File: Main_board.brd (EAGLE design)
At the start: 77.5 x 67.3 mm, 65 parts, among them U2 TPS61200, U3 MAX1704X, U4 USD-SOCKETNEW, U5 TPS61200, X1 USB-MICROB, Y1 16MHz KX-7

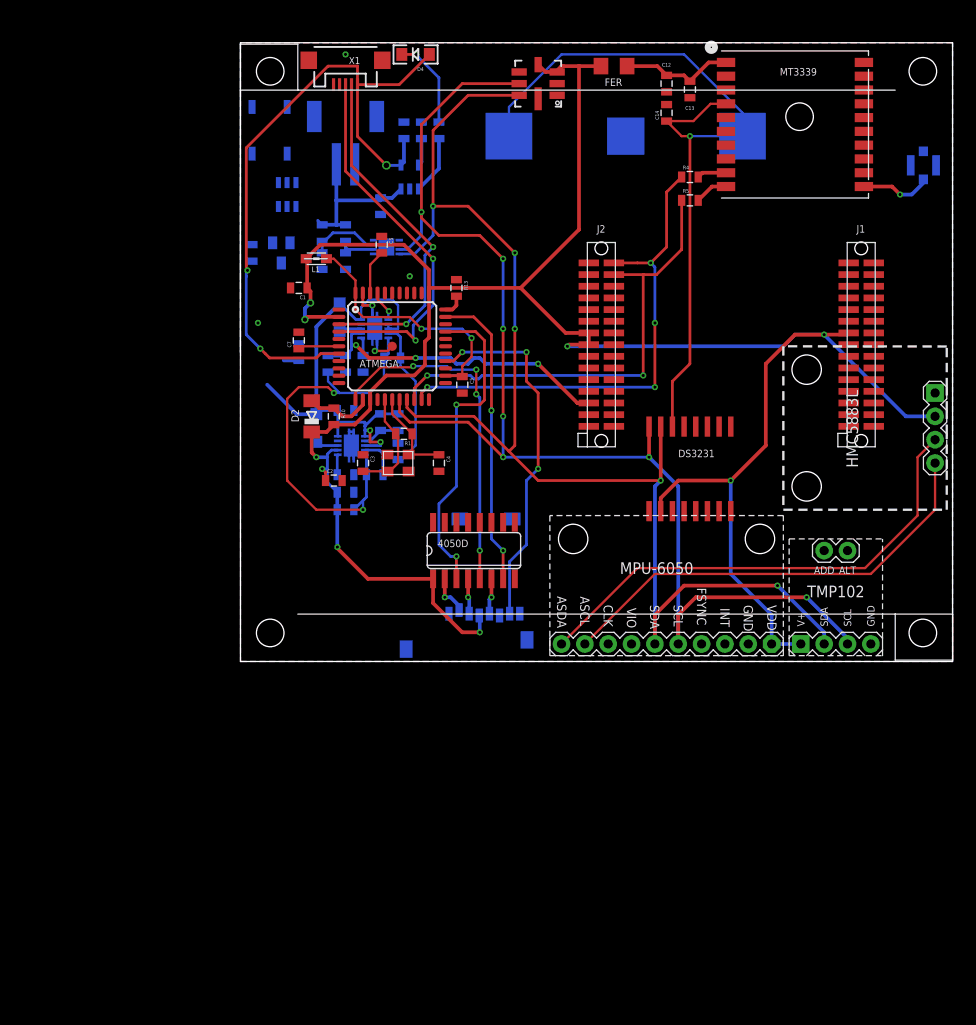
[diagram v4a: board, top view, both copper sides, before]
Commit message: 3V3 boost converter replacement
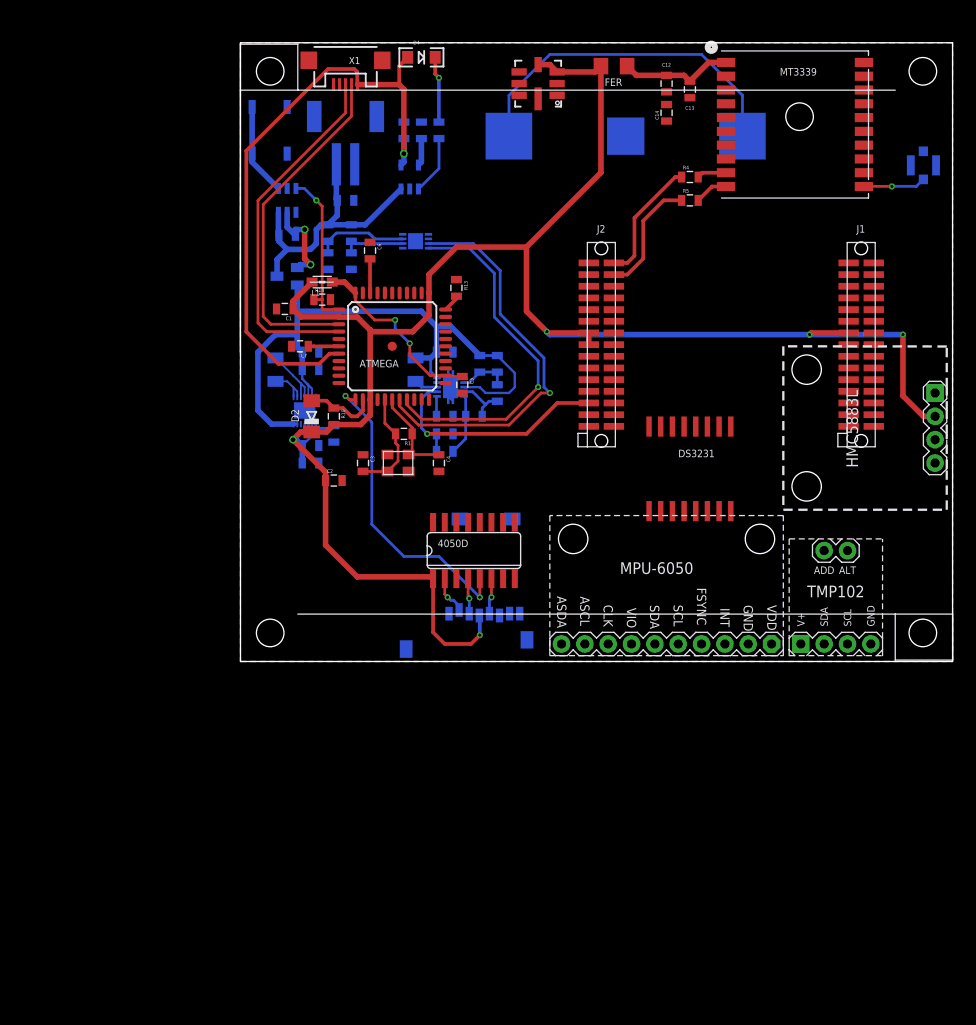
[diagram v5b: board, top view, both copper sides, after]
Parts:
- removed C22: 22uF, SparkFun:0805
- removed C24: 0.1uF, SparkFun:0805
- removed L3: 4.7uH, 1.2A, SparkFun:CDRH2D09
- removed R20: 2M, SparkFun:0805
- removed R21: 220k, SparkFun:0805
- removed U5: TPS61200, SparkFun:QFN-10_PAD
- added C19, C20, C21, C23: 22uF, SparkFun:0805
- added C25: 0.1uF, SparkFun:0805
- added L4: 4.7uH, 1.2A, rcl:2520
- added MAX16054: MAX16054, maxim:SOT23-6L
- L2: device SparkFun:CDRH2D09 -> rcl:2520
- R7: value 1.2M -> 2M
- U$9: value MAX16054 -> MAX8625A; device maxim:SOT23-6L -> maxim:14-TDFN-EP
- moved U$9 23.6 mm to (6.99, 27.3), turned to 270 degrees
- moved C15 12.5 mm to (22.2, 26.7)
- moved C16 12.5 mm to (22.2, 33.7)
- moved C8 12.5 mm to (22.2, 24.8)
- moved L2 12.5 mm to (19.1, 31.8), turned to 270 degrees
- moved R6 12.5 mm to (27.9, 29.2)
- moved C11 12.5 mm to (26.0, 32.4)
- moved R3 12.5 mm to (27.9, 32.4)
- moved R7 12.5 mm to (22.2, 22.9)
- moved R8 12.5 mm to (25.4, 26.7)
- moved U2 12.5 mm to (22.9, 29.8)
- moved R18 6.25 mm to (8.89, 39.4), flipped to the top, turned to 0 degrees
- moved R11 4.26 mm to (5.08, 46.4), turned to 180 degrees
- moved C10 3.86 mm to (11.4, 50.2), turned to 180 degrees
- moved U3 3.24 mm to (19.1, 45.7)
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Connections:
- removed net N$16: L3.P$1, U5.3
- removed net N$17: C24.1, U5.1
- new net N$22: C25.1, U$9.P$9
- new net N$23: L4.P$1, U$9.P$2, U$9.P$3
- new net N$24: L4.P$2, U$9.P$4, U$9.P$5
- net 5V: now also C8.1, R7.2, U2.2; no longer C22.1, R20.2, U5.2
- net A5: now also U2.6; no longer U5.6
- net D7: now also MAX16054.3; no longer U$9.3
- net FB: no longer R20.1, R21.2, U5.10
- net GND: now also C19.2, C20.2, C21.2, C23.2, C25.2, MAX16054.2, U$9.P$12, U$9.P$13, U$9.P$8; no longer C22.2, C24.2, U$9.2, U5.11, U5.12, U5.13, U5.14, U5.15, U5.4
- net GND1: no longer R21.1, U5.9
- net N$15: now also MAX16054.1; no longer U$9.1
- net N$19: now also MAX16054.5; no longer U$9.4
- net VCC: now also C21.1, C23.1, U$9.P$10, U$9.P$11; no longer C8.1, R7.2, U$9.6, U2.2
- net VIN: now also C19.1, C20.1, U$9.P$14, U$9.P$15, U$9.P$6, U$9.P$7; no longer L3.P$2, U2.6, U5.5, U5.7, U5.8
- net V_BATT: now also MAX16054.6
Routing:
- net SDA: track 141.7 -> 39.6 mm, vias 5 -> 1
- net SCL: track 140.9 -> 43.9 mm, vias 7 -> 1
- net AUX_SDA: track 53.6 -> 0.00 mm
- net VCC: track 254.0 -> 203.8 mm, vias 9 -> 5
- net AUX_SCL: track 49.2 -> 0.00 mm
- net VEE: track 84.7 -> 38.0 mm, vias 1 -> 0
- net TX: track 54.8 -> 13.7 mm, vias 4 -> 0
- net IO12: track 39.5 -> 0.00 mm, vias 3 -> 0
- net FB: track 45.6 -> 6.62 mm, vias 2 -> 0
- net RX: track 51.8 -> 13.1 mm, vias 2 -> 0
- net IO10*: track 35.3 -> 0.00 mm, vias 2 -> 0
- net IO13*: track 32.9 -> 0.00 mm, vias 2 -> 0
- net VIN: track 51.9 -> 72.4 mm, vias 2 -> 0
- net GND1: track 22.7 -> 5.76 mm
- net D7: track 1.64 -> 17.6 mm, vias 0 -> 1
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
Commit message: Board routing + cleaning
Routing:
- net SDA: track 39.6 -> 131.9 mm, vias 1 -> 5
- net SCL: track 43.9 -> 125.4 mm, vias 1 -> 6
- net AUX_SDA: track 0.00 -> 49.8 mm, vias 0 -> 1
- net VEE: track 38.0 -> 86.8 mm, vias 0 -> 1
- net AUX_SCL: track 0.00 -> 46.3 mm, vias 0 -> 1
- net VCC: track 203.8 -> 249.7 mm, vias 5 -> 6
- net RX: track 13.1 -> 52.0 mm, vias 0 -> 2
- net IO12: track 0.00 -> 38.8 mm, vias 0 -> 1
- net IO10*: track 0.00 -> 38.6 mm, vias 0 -> 2
- net TX: track 13.7 -> 51.6 mm, vias 0 -> 2
- net IO13*: track 0.00 -> 36.3 mm, vias 0 -> 2
- net A5: track 0.00 -> 31.3 mm, vias 0 -> 3
- net GND: track 5.51 -> 6.46 mm
- net N$3: track 2.60 -> 3.25 mm
- net 5V: track 28.0 -> 28.5 mm

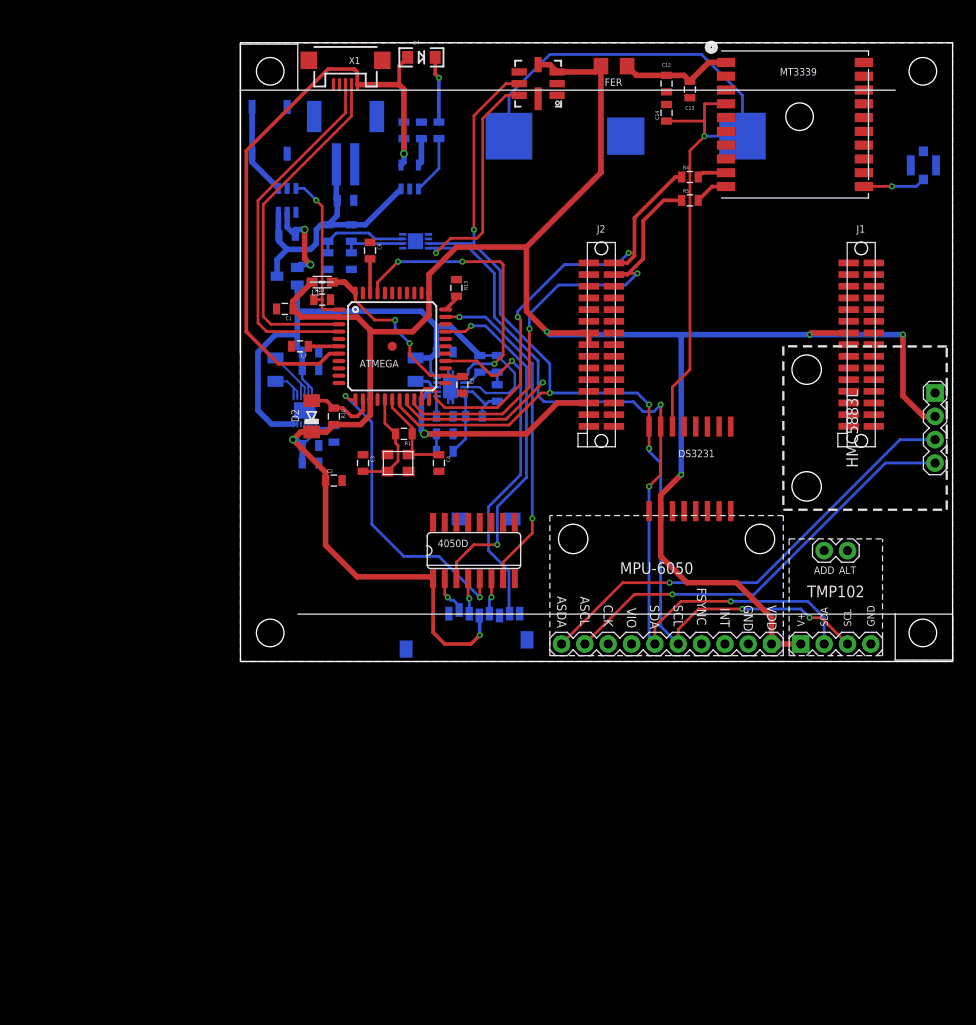
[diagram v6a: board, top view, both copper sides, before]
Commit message: Update to board
Alignement to grid, and thickness of traces adjuted
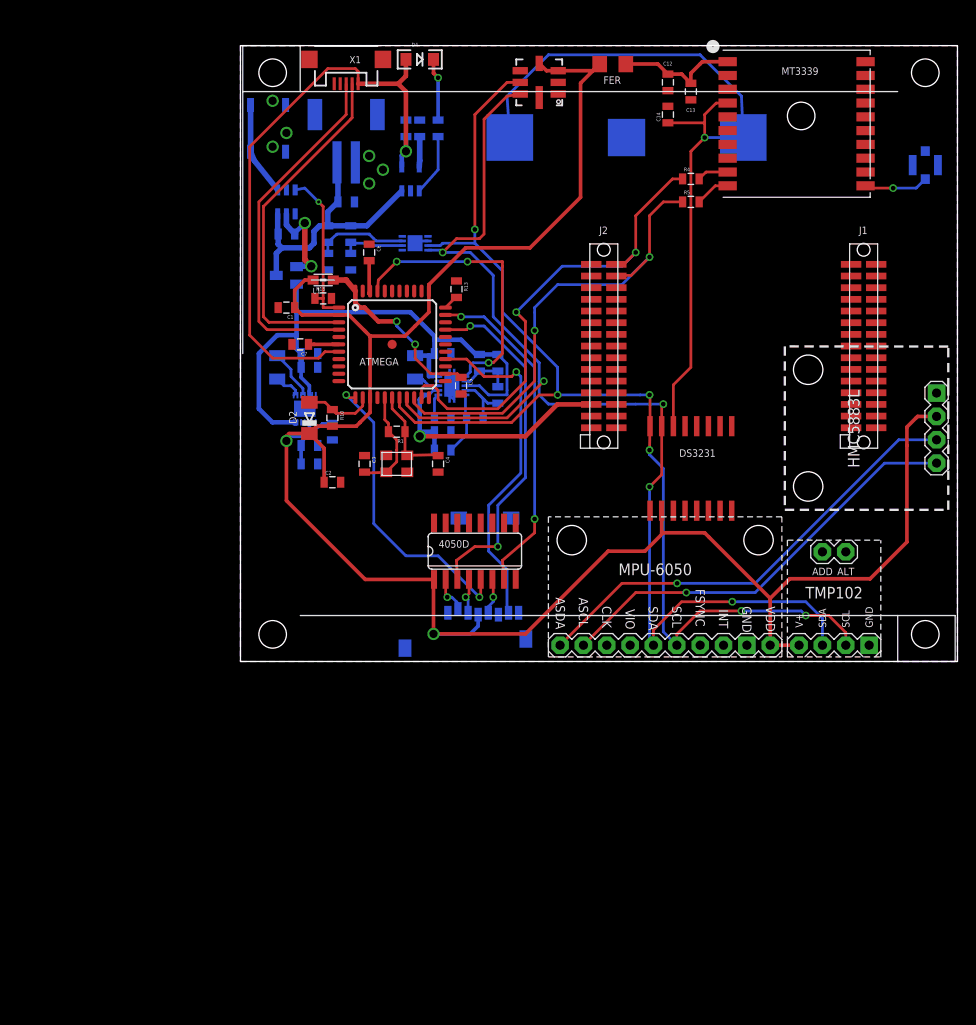
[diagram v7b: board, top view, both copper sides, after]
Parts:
- moved R1 0.81 mm to (17.0, 25.0)
- moved C8 0.33 mm to (22.0, 25.0)
- moved L4 0.31 mm to (4.00, 32.0)
- moved C9 0.31 mm to (18.0, 58.0)
- moved U$2 0.31 mm to (39.0, 33.5)
- moved D2 0.30 mm to (7.50, 26.5)
- moved D4 0.29 mm to (19.5, 65.5)
- moved C25 0.28 mm to (10.0, 25.0)
- moved R2 0.28 mm to (19.5, 58.0)
- moved C15 0.28 mm to (22.0, 26.5)
- moved C19 0.28 mm to (7.50, 32.0)
- moved S1 0.28 mm to (3.00, 58.0)
- moved C16 0.27 mm to (22.0, 33.5)
- moved FER 0.27 mm to (40.5, 65.0)
- moved R7 0.27 mm to (22.0, 23.0)
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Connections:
- net N$19 renamed V_CTRL
- new net J1-P18: U$2.J1-P18
- new net J2-P16: U$2.J2-P16
- new net J2-P18: U$2.J2-P18
- net VCC: no longer U$2.J1-P18, U$2.J2-P16, U$2.J2-P18
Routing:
- net VCC: track 249.7 -> 227.9 mm, vias 6 -> 2
- net SCL: track 125.4 -> 127.4 mm
- net VEE: track 86.8 -> 84.8 mm
- net 5V: track 28.5 -> 30.1 mm
- net SDA: track 131.9 -> 130.4 mm
- net VIN: track 72.4 -> 71.0 mm
- net IO12: track 38.8 -> 37.4 mm
- net N$9: track 12.3 -> 13.6 mm
- net N$23: track 4.70 -> 3.68 mm
- net GND1: track 5.76 -> 6.77 mm
- net N$24: track 7.03 -> 6.12 mm
- net TX: track 51.6 -> 52.3 mm
- net V_CTRL: track 10.2 -> 10.9 mm
- net VUSB: track 67.6 -> 66.9 mm
- net N$4: track 2.20 -> 2.70 mm
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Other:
- board size 77.5 x 67.3 mm -> 78 x 67 mm
